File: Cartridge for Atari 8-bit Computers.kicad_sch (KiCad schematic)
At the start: 15 parts, among them J1 Atari 8-bit Left Cartridge Co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, U0 27C128, U1 27C64, U2 74AHCT1G08

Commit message: Rename the project.
`Atari` being at the beginning of the name makes it seem like it's an
official project. Renaming should prevent any confusion.
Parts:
- U2: LCSC (none) -> C376056
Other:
- company: (none) -> Sean D. Cline
- title: (none) -> Atari 8-Bit (400/800/XL/XE) Cartridge
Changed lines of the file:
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@@
 	(generator_version "10.0")
 	(paper "A4")
+	(title_block
+		(title "Atari 8-Bit (400/800/XL/XE) Cartridge")
+		(date "2026-04-21")
+		(rev "1.0")
+		(company "Sean D. Cline")
+	)
 	(rectangle
 		(start 43.18 102.87)
@@
 		)
 		(instances
-			(project "Atari 8-bit Cartridge"
+			(project "Cartridge for Atari 8-bit Computers"
 				(path "/a4d58edd-db27-4f31-a98e-532286b289d0"
 					(reference "JP2")
@@
 		)
 		(instances
-			(project "Atari 8-bit Cartridge"
+			(project "Cartridge for Atari 8-bit Computers"
 				(path "/a4d58edd-db27-4f31-a98e-532286b289d0"
 					(reference "#PWR013")
@@
 		)
 		(instances
-			(project "Atari 8-bit Cartridge"
+			(project "Cartridge for Atari 8-bit Computers"
 				(path "/a4d58edd-db27-4f31-a98e-532286b289d0"
 					(reference "#PWR014")
@@
 		)
 		(instances
-			(project "Atari 8-bit Cartridge"
+			(project "Cartridge for Atari 8-bit Computers"
 				(path "/a4d58edd-db27-4f31-a98e-532286b289d0"
 					(reference "#PWR07")
@@
 		)
 		(instances
-			(project "Atari 8-bit Cartridge"
+			(project "Cartridge for Atari 8-bit Computers"
 				(path "/a4d58edd-db27-4f31-a98e-532286b289d0"
 					(reference "JP9")
@@
 		)
 		(instances
-			(project "Atari 8-bit Cartridge"
+			(project "Cartridge for Atari 8-bit Computers"
 				(path "/a4d58edd-db27-4f31-a98e-532286b289d0"
 					(reference "#PWR012")
@@
 		)
 		(instances
-			(project "Atari 8-bit Cartridge"
+			(project "Cartridge for Atari 8-bit Computers"
 				(path "/a4d58edd-db27-4f31-a98e-532286b289d0"
 					(reference "JP8")
@@
 		)
 		(instances
-			(project "Atari 8-bit Cartridge"
+			(project "Cartridge for Atari 8-bit Computers"
 				(path "/a4d58edd-db27-4f31-a98e-532286b289d0"
 					(reference "#PWR018")
@@
 		)
 		(instances
-			(project "Atari 8-bit Cartridge"
+			(project "Cartridge for Atari 8-bit Computers"
 				(path "/a4d58edd-db27-4f31-a98e-532286b289d0"
 					(reference "#PWR010")
@@
 		)
 		(instances
-			(project "Atari 8-bit Cartridge"
+			(project "Cartridge for Atari 8-bit Computers"
 				(path "/a4d58edd-db27-4f31-a98e-532286b289d0"
 					(reference "J1")
@@
 		)
 		(instances
-			(project "Atari 8-bit Cartridge"
+			(project "Cartridge for Atari 8-bit Computers"
 				(path "/a4d58edd-db27-4f31-a98e-532286b289d0"
 					(reference "#PWR016")
@@
 		)
 		(instances
-			(project "Atari 8-bit Cartridge"
+			(project "Cartridge for Atari 8-bit Computers"
 				(path "/a4d58edd-db27-4f31-a98e-532286b289d0"
 					(reference "JP6")
@@
 		)
 		(instances
-			(project "Atari 8-bit Cartridge"
+			(project "Cartridge for Atari 8-bit Computers"
 				(path "/a4d58edd-db27-4f31-a98e-532286b289d0"
 					(reference "#PWR09")
@@
 		)
 		(instances
-			(project "Atari 8-bit Cartridge"
+			(project "Cartridge for Atari 8-bit Computers"
 				(path "/a4d58edd-db27-4f31-a98e-532286b289d0"
 					(reference "#PWR011")
@@
 		)
 		(instances
-			(project "Atari 8-bit Cartridge"
+			(project "Cartridge for Atari 8-bit Computers"
 				(path "/a4d58edd-db27-4f31-a98e-532286b289d0"
 					(reference "#PWR05")
@@
 		)
 		(instances
-			(project "Atari 8-bit Cartridge"
+			(project "Cartridge for Atari 8-bit Computers"
 				(path "/a4d58edd-db27-4f31-a98e-532286b289d0"
 					(reference "#PWR019")
@@
 		)
 		(instances
-			(project "Atari 8-bit Cartridge"
+			(project "Cartridge for Atari 8-bit Computers"
 				(path "/a4d58edd-db27-4f31-a98e-532286b289d0"
 					(reference "#PWR04")
@@
 		)
 		(instances
-			(project "Atari 8-bit Cartridge"
+			(project "Cartridge for Atari 8-bit Computers"
 				(path "/a4d58edd-db27-4f31-a98e-532286b289d0"
 					(reference "#PWR08")
@@
 		)
 		(instances
-			(project "Atari 8-bit Cartridge"
+			(project "Cartridge for Atari 8-bit Computers"
 				(path "/a4d58edd-db27-4f31-a98e-532286b289d0"
 					(reference "JP4")
@@
 		)
 		(instances
-			(project "Atari 8-bit Cartridge"
+			(project "Cartridge for Atari 8-bit Computers"
 				(path "/a4d58edd-db27-4f31-a98e-532286b289d0"
 					(reference "#PWR03")
@@
 			)
 		)
+		(property "LCSC" "C376056"
+			(at 63.5 149.86 0)
+			(hide yes)
+			(show_name no)
+			(do_not_autoplace no)
+			(effects
+				(font
+					(size 1.27 1.27)
+				)
+			)
+		)
 		(pin "2"
 		)
@@
 		)
 		(instances
-			(project "Atari 8-bit Cartridge"
+			(project "Cartridge for Atari 8-bit Computers"
 				(path "/a4d58edd-db27-4f31-a98e-532286b289d0"
 					(reference "U2")
@@
 		)
 		(instances
-			(project "Atari 8-bit Cartridge"
+			(project "Cartridge for Atari 8-bit Computers"
 				(path "/a4d58edd-db27-4f31-a98e-532286b289d0"
 					(reference "JP5")
@@
 		)
 		(instances
-			(project "Atari 8-bit Cartridge"
+			(project "Cartridge for Atari 8-bit Computers"
 				(path "/a4d58edd-db27-4f31-a98e-532286b289d0"
 					(reference "JP3")
@@
 		)
 		(instances
-			(project "Atari 8-bit Cartridge"
+			(project "Cartridge for Atari 8-bit Computers"
 				(path "/a4d58edd-db27-4f31-a98e-532286b289d0"
 					(reference "C1")
@@
 		)
 		(instances
-			(project "Atari 8-bit Cartridge"
+			(project "Cartridge for Atari 8-bit Computers"
 				(path "/a4d58edd-db27-4f31-a98e-532286b289d0"
 					(reference "#PWR06")
@@
 		)
 		(instances
-			(project "Atari 8-bit Cartridge"
+			(project "Cartridge for Atari 8-bit Computers"
 				(path "/a4d58edd-db27-4f31-a98e-532286b289d0"
 					(reference "U0")
@@
 		)
 		(instances
-			(project "Atari 8-bit Cartridge"
+			(project "Cartridge for Atari 8-bit Computers"
 				(path "/a4d58edd-db27-4f31-a98e-532286b289d0"
 					(reference "#PWR01")
@@
 		)
 		(instances
-			(project "Atari 8-bit Cartridge"
+			(project "Cartridge for Atari 8-bit Computers"
 				(path "/a4d58edd-db27-4f31-a98e-532286b289d0"
 					(reference "JP1")
@@
 		)
 		(instances
-			(project "Atari 8-bit Cartridge"
+			(project "Cartridge for Atari 8-bit Computers"
 				(path "/a4d58edd-db27-4f31-a98e-532286b289d0"
 					(reference "#PWR015")
@@
 		)
 		(instances
-			(project "Atari 8-bit Cartridge"
+			(project "Cartridge for Atari 8-bit Computers"
 				(path "/a4d58edd-db27-4f31-a98e-532286b289d0"
 					(reference "C0")
@@
 		)
 		(instances
-			(project "Atari 8-bit Cartridge"
+			(project "Cartridge for Atari 8-bit Computers"
 				(path "/a4d58edd-db27-4f31-a98e-532286b289d0"
 					(reference "U1")
@@
 		)
 		(instances
-			(project "Atari 8-bit Cartridge"
+			(project "Cartridge for Atari 8-bit Computers"
 				(path "/a4d58edd-db27-4f31-a98e-532286b289d0"
 					(reference "#PWR02")
@@
 		)
 		(instances
-			(project "Atari 8-bit Cartridge"
+			(project "Cartridge for Atari 8-bit Computers"
 				(path "/a4d58edd-db27-4f31-a98e-532286b289d0"
 					(reference "#PWR017")
@@
 		)
 		(instances
-			(project "Atari 8-bit Cartridge"
+			(project "Cartridge for Atari 8-bit Computers"
 				(path "/a4d58edd-db27-4f31-a98e-532286b289d0"
 					(reference "JP7")

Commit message: Add LCSC component part numbers for assembly.
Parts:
- C0, C1: LCSC (none) -> C2896060
- U0, U1: LCSC (none) -> C72121
- U2: LCSC C376056 -> C460499
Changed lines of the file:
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@@
 			)
 		)
-		(property "LCSC" "C376056"
+		(property "LCSC" "C460499"
 			(at 63.5 149.86 0)
 			(hide yes)
@@
 			)
 		)
+		(property "LCSC" "C2896060"
+			(at 125.73 22.86 90)
+			(hide yes)
+			(show_name no)
+			(do_not_autoplace no)
+			(effects
+				(font
+					(size 1.27 1.27)
+				)
+			)
+		)
 		(pin "2"
 		)
@@
 			)
 		)
+		(property "LCSC" "C72121"
+			(at 190.5 64.77 0)
+			(hide yes)
+			(show_name no)
+			(do_not_autoplace no)
+			(effects
+				(font
+					(size 1.27 1.27)
+				)
+			)
+		)
 		(pin "10"
 		)
@@
 			)
 		)
+		(property "LCSC" "C2896060"
+			(at 190.5 22.86 90)
+			(hide yes)
+			(show_name no)
+			(do_not_autoplace no)
+			(effects
+				(font
+					(size 1.27 1.27)
+				)
+			)
+		)
 		(pin "2"
 		)
@@
 			(at 125.73 62.23 0)
 			(hide yes)
+			(show_name no)
+			(do_not_autoplace no)
+			(effects
+				(font
+					(size 1.27 1.27)
+				)
+			)
+		)
+		(property "LCSC" "C72121"
+			(at 125.73 62.23 0)
+			(hide yes)

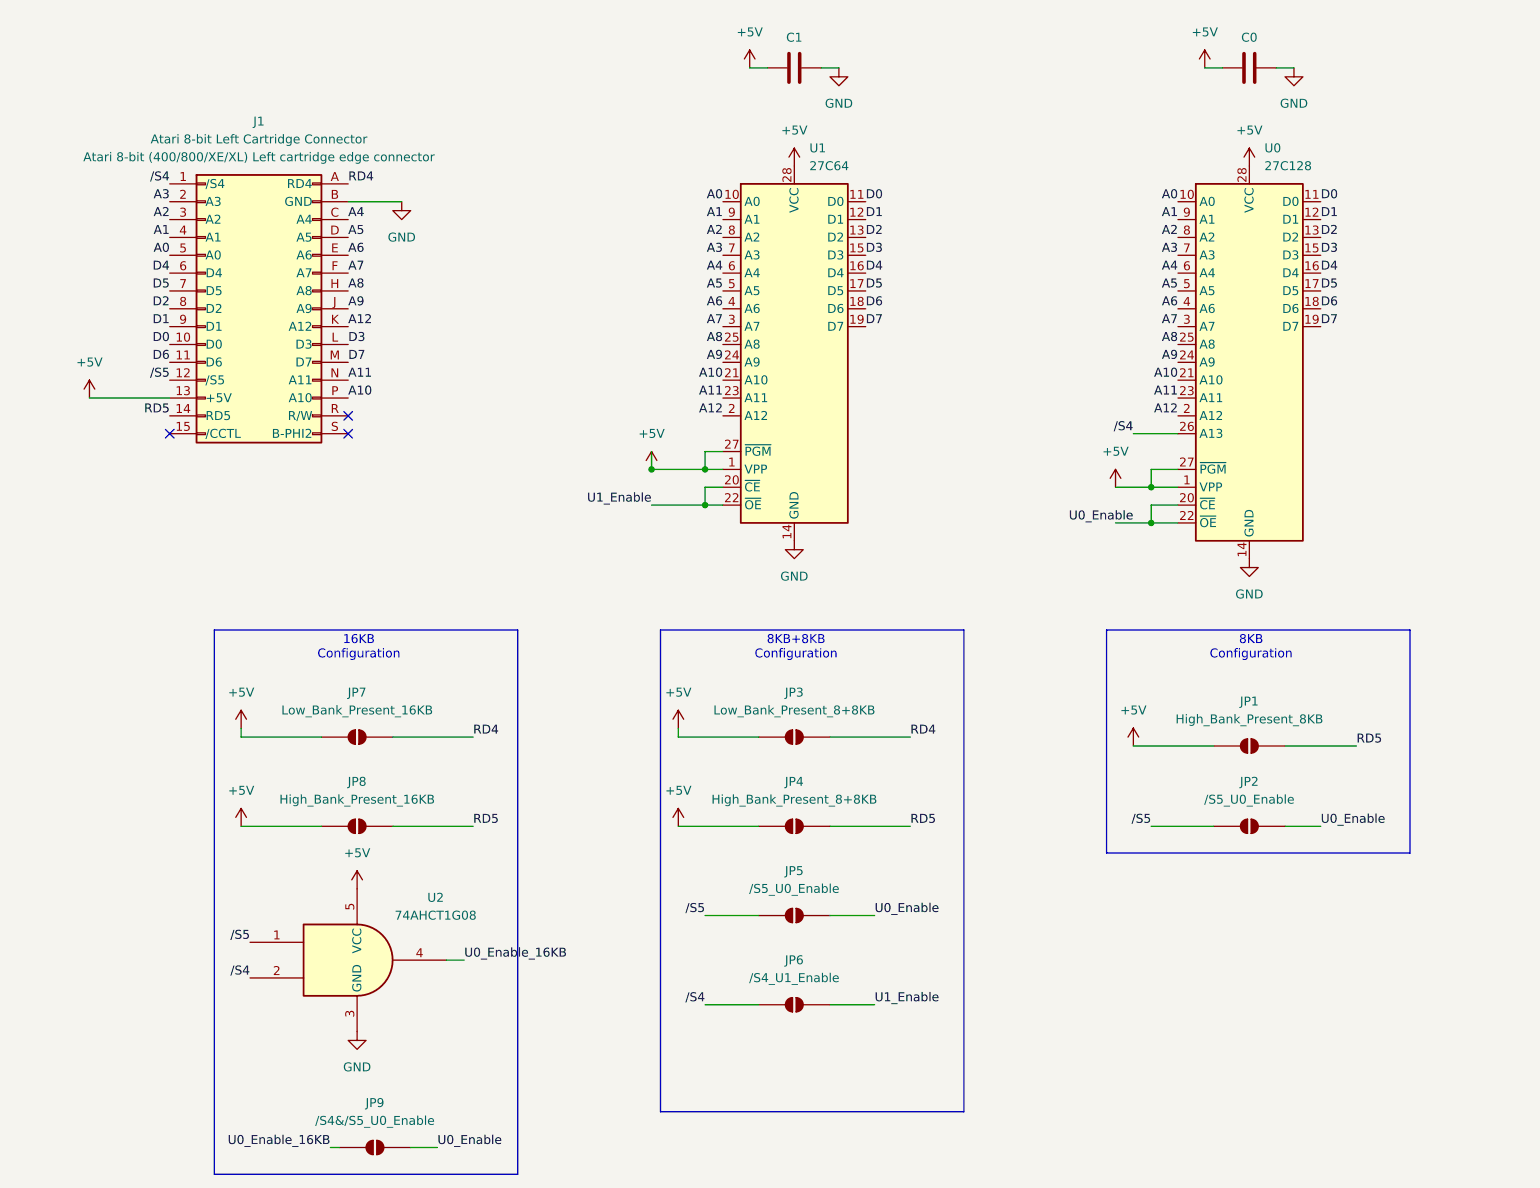
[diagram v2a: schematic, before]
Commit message: Allow through-hole components when generating the BOM/CPL.
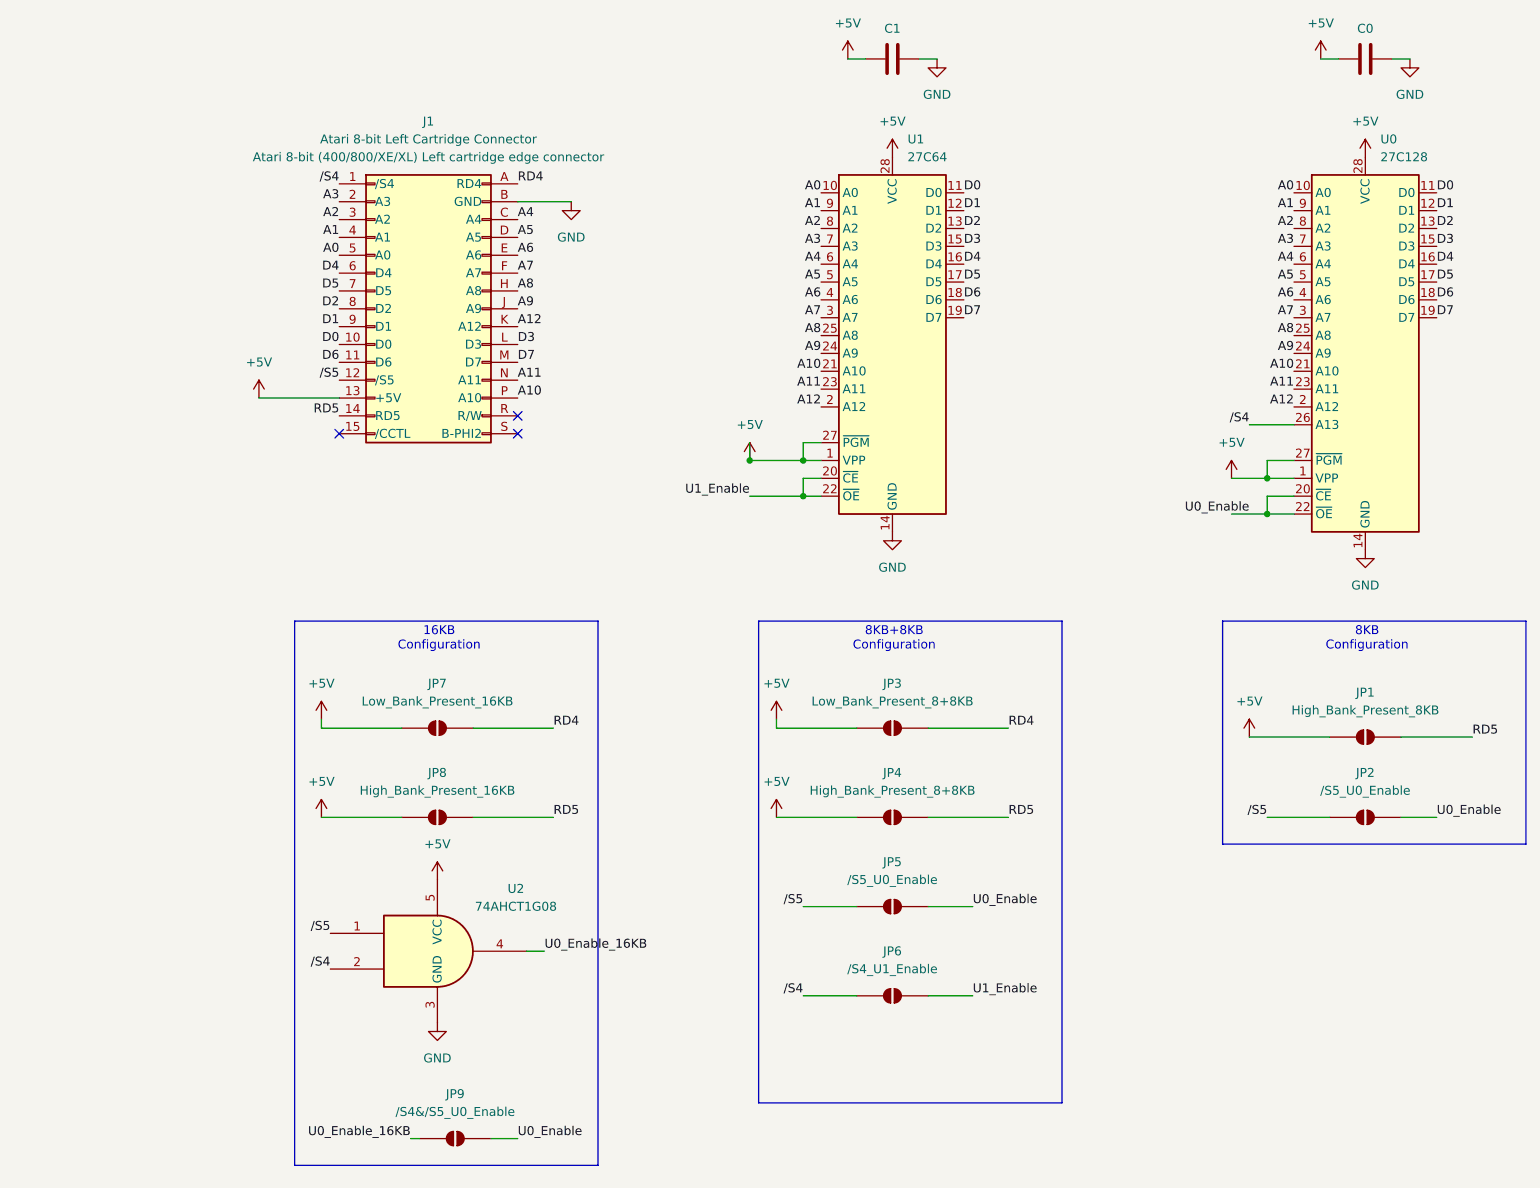
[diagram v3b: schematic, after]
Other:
- title: Atari 8-Bit (400/800/XL/XE) Cartridge -> Cartridge for Atari 8-Bit Computers (400/800/XL/XE) 
- moved on the sheet: C0, C1, J1, JP1, JP2, JP3, JP4, JP5, JP6, JP7, JP8, JP9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
